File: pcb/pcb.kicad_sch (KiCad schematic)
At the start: 3 parts, among them U1 ESP32-DEVKIT-V1, U3 ZC323200, U4 GY-521

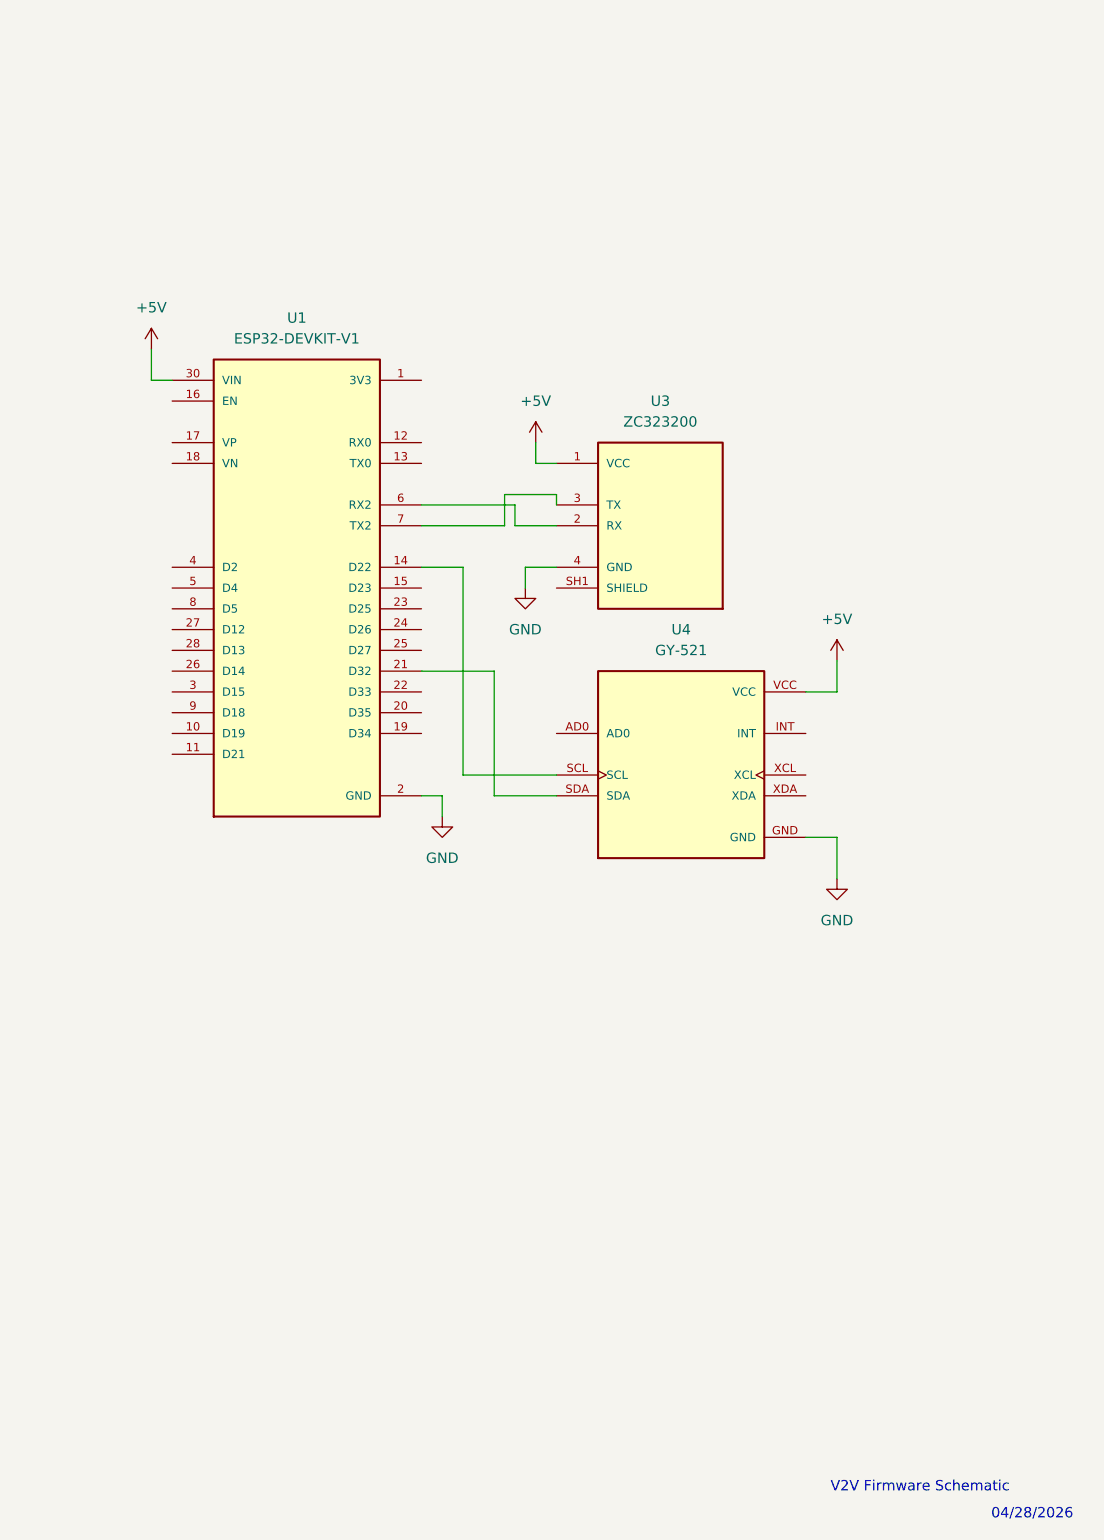
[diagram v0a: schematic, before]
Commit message: suporte a DWM1000 e PCB
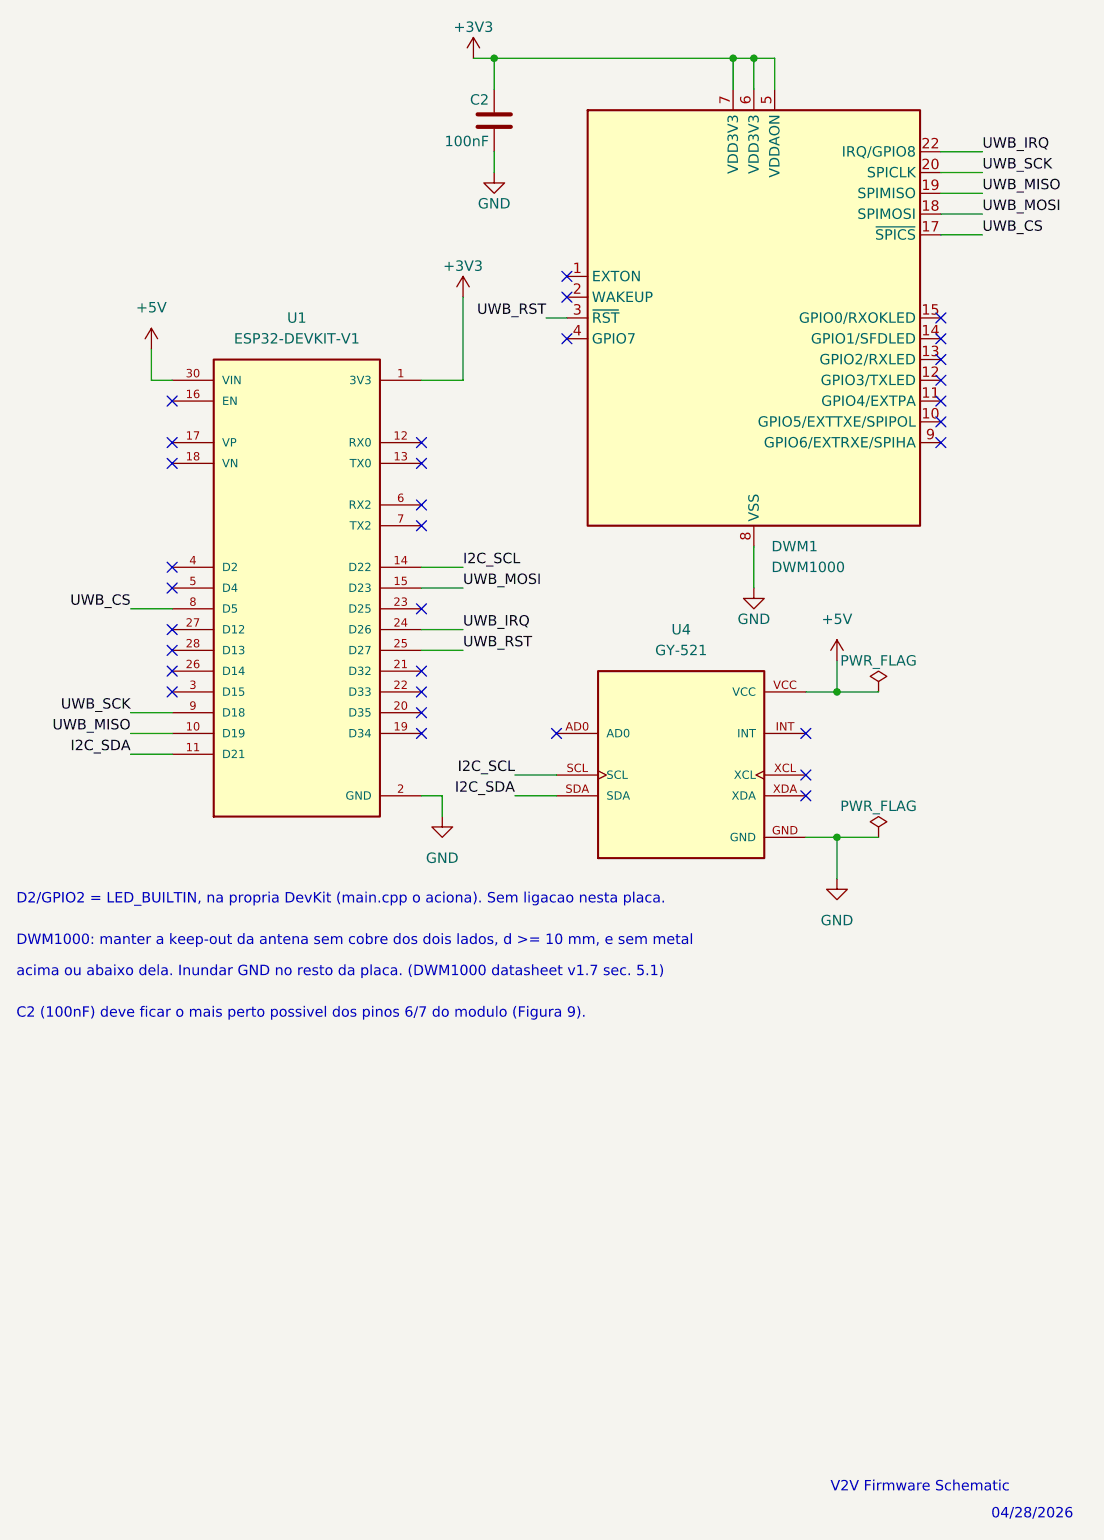
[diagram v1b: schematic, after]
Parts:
- removed U3: ZC323200, ZC323200:XCVR_ZC323200, symbol ZC323200:ZC323200
- added C2: 100nF, Capacitor_SMD:C_0805_2012Metric, symbol Device:C
- added DWM1: DWM1000, RF_Module:DWM1000, symbol RF_Module:DWM1000
- U1: footprint ESP32-DEVKIT-V1:MODULE_ESP32_DEVKIT_V1 -> esp32:MODULE_ESP32_DEVKIT_V1
- U4: footprint GY-521:MODULE_GY-521 -> gy-521:MODULE_GY-521
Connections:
- net GND: now also C2.2, DWM1.16 (VSS), DWM1.21 (VSS), DWM1.23 (VSS), DWM1.24 (VSS), DWM1.8 (VSS)
- net +3V3: now reaches U1.1 (3V3)
- net +3V3: now also C2.1, DWM1.5 (VDDAON), DWM1.6 (VDD3V3), DWM1.7 (VDD3V3)
- net UWB_MISO: now reaches U1.10 (D19)
- net UWB_MISO: now also DWM1.19 (SPIMISO)
- net I2C_SDA: now reaches U1.11 (D21)
- net I2C_SDA: now also U4.SDA
- net I2C_SCL: now reaches U1.14 (D22), U4.SCL
- net UWB_MOSI: now reaches U1.15 (D23)
- net UWB_MOSI: now also DWM1.18 (SPIMOSI)
- net at U1.21 (D32): no longer U4.SDA
- net UWB_IRQ: now reaches U1.24 (D26)
- net UWB_IRQ: now also DWM1.22 (IRQ/GPIO8)
- net UWB_RST: now reaches U1.25 (D27)
- net UWB_RST: now also DWM1.3 (~{RST})
- net UWB_CS: now reaches U1.8 (D5)
- net UWB_CS: now also DWM1.17 (~{SPICS})
- net UWB_SCK: now reaches U1.9 (D18)
- net UWB_SCK: now also DWM1.20 (SPICLK)
- no-connect marks 0 -> 32
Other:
- note added: "C2 (100nF) deve ficar o mais perto possivel dos pinos 6/7 do modulo (Figura 9)."
- note added: "D2/GPIO2 = LED_BUILTIN, na propria DevKit (main.cpp o aciona). Sem ligacao nesta placa."
- note added: "DWM1000: manter a keep-out da antena sem cobre dos dois lados, d >= 10 mm, e sem metal"
- note added: "acima ou abaixo dela. Inundar GND no resto da placa. (DWM1000 datasheet v1.7 sec. 5.1)"
